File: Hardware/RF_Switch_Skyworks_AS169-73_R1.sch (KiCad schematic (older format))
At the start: 5 parts, among them U7 AS169-73

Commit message: Added discrete Chebyshev input filter to schematic based on Qucs simulationd. Artwork not done. It has occurred to me that I need to do some major cleanup of the test points on this PCBA.
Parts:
- renumbered C42 to C41, C43 to C42, C44 to C43
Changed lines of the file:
@@
 $Descr A4 11693 8268
 encoding utf-8
-Sheet 12 12
+Sheet 12 16
 Title ""
 Date ""
@@
 AR Path="/5F20D989/5F02EBC3" Ref="#PWR?"  Part="1"
 AR Path="/5F20DB0B/5F02EBC3" Ref="#PWR?"  Part="1"
-AR Path="/5F2751D2/5F02EBC3" Ref="#PWR051"  Part="1"
-F 0 "#PWR051" H 5600 3850 50  0001 C CNN
+AR Path="/5F2751D2/5F02EBC3" Ref="#PWR048"  Part="1"
+F 0 "#PWR048" H 5600 3850 50  0001 C CNN
 F 1 "GNDA" H 5605 3927 50  0000 C CNN
 F 2 "" H 5600 4100 50  0001 C CNN
@@
 AR Path="/5F20D989/5F11A2FE" Ref="C?"  Part="1"
 AR Path="/5F20DB0B/5F11A2FE" Ref="C?"  Part="1"
-AR Path="/5F2751D2/5F11A2FE" Ref="C42"  Part="1"
-F 0 "C42" V 4498 3400 50  0000 C CNN
+AR Path="/5F2751D2/5F11A2FE" Ref="C41"  Part="1"
+F 0 "C41" V 4498 3400 50  0000 C CNN
 F 1 "600S101" V 4589 3400 50  0000 C CNN
 F 2 "Capacitor_SMD:C_0603_1608Metric" H 4800 3500 50  0001 C CNN
@@
 AR Path="/5F20D989/5F30C645" Ref="#PWR?"  Part="1"
 AR Path="/5F20DB0B/5F30C645" Ref="#PWR?"  Part="1"
-AR Path="/5F2751D2/5F30C645" Ref="#PWR052"  Part="1"
-F 0 "#PWR052" H 6900 2550 50  0001 C CNN
+AR Path="/5F2751D2/5F30C645" Ref="#PWR049"  Part="1"
+F 0 "#PWR049" H 6900 2550 50  0001 C CNN
 F 1 "GNDA" H 6905 2627 50  0000 C CNN
 F 2 "" H 6900 2800 50  0001 C CNN
@@
 AR Path="/5F20D989/5F30E7E0" Ref="C?"  Part="1"
 AR Path="/5F20DB0B/5F30E7E0" Ref="C?"  Part="1"
-AR Path="/5F2751D2/5F30E7E0" Ref="C43"  Part="1"
-F 0 "C43" V 6400 3700 50  0000 C CNN
+AR Path="/5F2751D2/5F30E7E0" Ref="C42"  Part="1"
+F 0 "C42" V 6400 3700 50  0000 C CNN
 F 1 "600S101" V 6500 3700 50  0000 C CNN
 F 2 "Capacitor_SMD:C_0603_1608Metric" H 6300 3800 50  0001 C CNN
@@
 J2
 $Comp
-L ATC:600S101_3-pad-R C44
+L ATC:600S101_3-pad-R C43
 U 1 1 5F334699
 P 6500 3300
-F 0 "C44" H 6150 3450 50  0000 L CNN
+F 0 "C43" H 6150 3450 50  0000 L CNN
 F 1 "600S101_3-pad-R" H 6150 3550 50  0000 L CNN
 F 2 "Capacitor_SMD:C_0603_1608Metric_3-pad-R" H 7400 2550 50  0001 C CNN

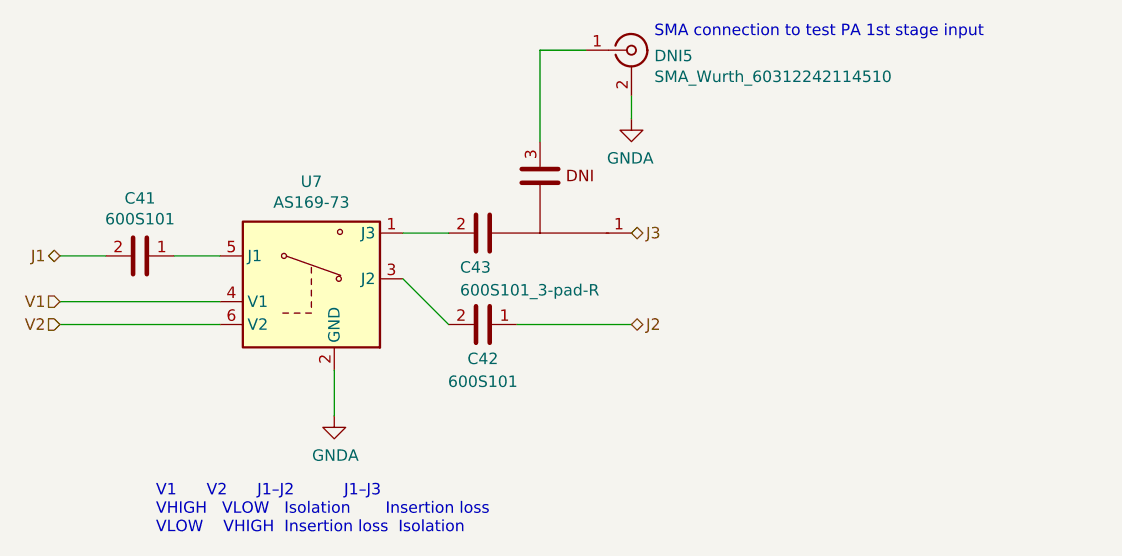
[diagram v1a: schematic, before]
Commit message: Major cleanup to both the schematic and directory structure. Stackup has changed accomodate to 0.65mm trace width. Chebyshev filter lived through the experience in the Qucs simulation; others not checked yet. I do want to re-visit the matching networks of all of the amplifiers as I have developed some good strategies to implement them.
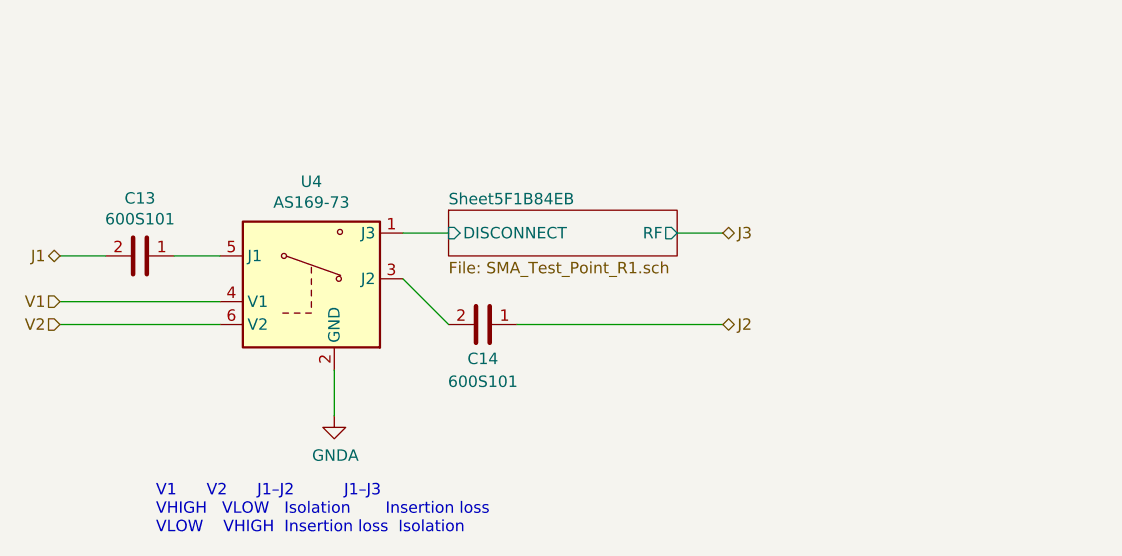
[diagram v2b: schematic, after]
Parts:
- removed C43: 600S101_3-pad-R, Capacitor_SMD:C_0603_1608Metric_3-pad-R, symbol ATC:600S101_3-pad-R
- removed DNI5: SMA_Wurth_60312242114510, RF:SMA_Wurth_60312242114510, symbol RF:SMA_Wurth_60312242114510
- renumbered C41 to C13, C42 to C14, U7 to U4
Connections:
- net Sheet5F1B84EB/DISCONNECT: now reaches U4.1 (J3)
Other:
- note removed: "SMA connection to test PA 1st stage input"
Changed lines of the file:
@@
 $Descr A4 11693 8268
 encoding utf-8
-Sheet 12 16
+Sheet 15 24
 Title ""
 Date ""
@@
 AR Path="/5F20D989/5F02EBC3" Ref="#PWR?"  Part="1"
 AR Path="/5F20DB0B/5F02EBC3" Ref="#PWR?"  Part="1"
-AR Path="/5F2751D2/5F02EBC3" Ref="#PWR048"  Part="1"
-F 0 "#PWR048" H 5600 3850 50  0001 C CNN
+AR Path="/5F2751D2/5F02EBC3" Ref="#PWR017"  Part="1"
+F 0 "#PWR017" H 5600 3850 50  0001 C CNN
 F 1 "GNDA" H 5605 3927 50  0000 C CNN
 F 2 "" H 5600 4100 50  0001 C CNN
@@
 AR Path="/5F20D989/5F064460" Ref="U?"  Part="1"
 AR Path="/5F20DB0B/5F064460" Ref="U?"  Part="1"
-AR Path="/5F2751D2/5F064460" Ref="U7"  Part="1"
-F 0 "U7" H 5500 3925 50  0000 C CNN
+AR Path="/5F2751D2/5F064460" Ref="U4"  Part="1"
+F 0 "U4" H 5500 3925 50  0000 C CNN
 F 1 "AS169-73" H 5500 3834 50  0000 C CNN
 F 2 "Package_TO_SOT_SMD:SOT-23-6" H 5600 3500 50  0001 C CNN
@@
 AR Path="/5F20D989/5F11A2FE" Ref="C?"  Part="1"
 AR Path="/5F20DB0B/5F11A2FE" Ref="C?"  Part="1"
-AR Path="/5F2751D2/5F11A2FE" Ref="C41"  Part="1"
-F 0 "C41" V 4498 3400 50  0000 C CNN
+AR Path="/5F2751D2/5F11A2FE" Ref="C13"  Part="1"
+F 0 "C13" V 4498 3400 50  0000 C CNN
 F 1 "600S101" V 4589 3400 50  0000 C CNN
 F 2 "Capacitor_SMD:C_0603_1608Metric" H 4800 3500 50  0001 C CNN
@@
 $EndComp
 Wire Wire Line
-	6700 2500 6500 2500
-Text Notes 7000 2450 0    50   ~ 0
-SMA connection to test PA 1st stage input
-$Comp
-L RF:SMA_Wurth_60312242114510 DNI?
-U 1 1 5F30C63E
-P 6900 2500
-AR Path="/5F20DB0B/5F30C63E" Ref="DNI?"  Part="1"
-AR Path="/5F20A94F/5F30C63E" Ref="DNI?"  Part="1"
-AR Path="/5F2751D2/5F30C63E" Ref="DNI5"  Part="1"
-F 0 "DNI5" H 7000 2475 50  0000 L CNN
-F 1 "SMA_Wurth_60312242114510" H 7000 2384 50  0000 L CNN
-F 2 "RF:SMA_Wurth_60312242114510" H 6900 2500 50  0001 C CNN
-F 3 "https://www.we-online.de/katalog/datasheet/60312242114510.pdf" H 6900 2500 50  0001 C CNN
-	1    6900 2500
-	1    0    0    -1
-$EndComp
-$Comp
-L power:GNDA #PWR?
-U 1 1 5F30C645
-P 6900 2800
-AR Path="/5F1FE880/5F30C645" Ref="#PWR?"  Part="1"
-AR Path="/5F19C733/5F30C645" Ref="#PWR?"  Part="1"
-AR Path="/5F19DDB3/5F30C645" Ref="#PWR?"  Part="1"
-AR Path="/5F11BFA6/5F30C645" Ref="#PWR?"  Part="1"
-AR Path="/5F11C68E/5F30C645" Ref="#PWR?"  Part="1"
-AR Path="/5F20A94F/5F30C645" Ref="#PWR?"  Part="1"
-AR Path="/5F20D989/5F30C645" Ref="#PWR?"  Part="1"
-AR Path="/5F20DB0B/5F30C645" Ref="#PWR?"  Part="1"
-AR Path="/5F2751D2/5F30C645" Ref="#PWR049"  Part="1"
-F 0 "#PWR049" H 6900 2550 50  0001 C CNN
-F 1 "GNDA" H 6905 2627 50  0000 C CNN
-F 2 "" H 6900 2800 50  0001 C CNN
-F 3 "" H 6900 2800 50  0001 C CNN
-	1    6900 2800
-	-1   0    0    -1
-$EndComp
-Wire Wire Line
-	6900 2700 6900 2800
-Wire Wire Line
-	6500 2500 6500 2900
-Wire Wire Line
 	5900 3500 6100 3700
-Text HLabel 6900 3300 2    50   BiDi ~ 0
+Text HLabel 7300 3300 2    50   BiDi ~ 0
 J3
-Wire Wire Line
-	6400 3700 6900 3700
 $Comp
 L ATC:600S101 C?
@@
 AR Path="/5F20D989/5F30E7E0" Ref="C?"  Part="1"
 AR Path="/5F20DB0B/5F30E7E0" Ref="C?"  Part="1"
-AR Path="/5F2751D2/5F30E7E0" Ref="C42"  Part="1"
-F 0 "C42" V 6400 3700 50  0000 C CNN
+AR Path="/5F2751D2/5F30E7E0" Ref="C14"  Part="1"
+F 0 "C14" V 6400 3700 50  0000 C CNN
 F 1 "600S101" V 6500 3700 50  0000 C CNN
 F 2 "Capacitor_SMD:C_0603_1608Metric" H 6300 3800 50  0001 C CNN
@@
 	0    1    1    0
 $EndComp
-Text HLabel 6900 3700 2    50   BiDi ~ 0
+Text HLabel 7300 3700 2    50   BiDi ~ 0
 J2
-$Comp
-L ATC:600S101_3-pad-R C43
-U 1 1 5F334699
-P 6500 3300
-F 0 "C43" H 6150 3450 50  0000 L CNN
-F 1 "600S101_3-pad-R" H 6150 3550 50  0000 L CNN
-F 2 "Capacitor_SMD:C_0603_1608Metric_3-pad-R" H 7400 2550 50  0001 C CNN
-F 3 "" V 6500 3250 50  0001 C CNN
-	1    6500 3300
-	1    0    0    1
-$EndComp
+Wire Wire Line
+	6400 3700 7300 3700
+Wire Wire Line
+	7100 3300 7300 3300
+$Sheet
+S 6100 3200 1000 200
+U 5F1B84EC
+F0 "Sheet5F1B84EB" 50
+F1 "SMA_Test_Point_R1.sch" 50
+F2 "DISCONNECT" I L 6100 3300 50
+F3 "RF" O R 7100 3300 50
+$EndSheet
 $EndSCHEMATC

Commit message: Improving LNA simulations and Documentation package. More to come on this one.
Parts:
- renumbered C13 to C16, C14 to C17
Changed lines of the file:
@@
 $Descr A4 11693 8268
 encoding utf-8
-Sheet 15 24
+Sheet 8 23
 Title ""
 Date ""
@@
 AR Path="/5F20D989/5F02EBC3" Ref="#PWR?"  Part="1"
 AR Path="/5F20DB0B/5F02EBC3" Ref="#PWR?"  Part="1"
-AR Path="/5F2751D2/5F02EBC3" Ref="#PWR017"  Part="1"
-F 0 "#PWR017" H 5600 3850 50  0001 C CNN
+AR Path="/5F2751D2/5F02EBC3" Ref="#PWR019"  Part="1"
+F 0 "#PWR019" H 5600 3850 50  0001 C CNN
 F 1 "GNDA" H 5605 3927 50  0000 C CNN
 F 2 "" H 5600 4100 50  0001 C CNN
@@
 AR Path="/5F20D989/5F11A2FE" Ref="C?"  Part="1"
 AR Path="/5F20DB0B/5F11A2FE" Ref="C?"  Part="1"
-AR Path="/5F2751D2/5F11A2FE" Ref="C13"  Part="1"
-F 0 "C13" V 4498 3400 50  0000 C CNN
+AR Path="/5F2751D2/5F11A2FE" Ref="C16"  Part="1"
+F 0 "C16" V 4498 3400 50  0000 C CNN
 F 1 "600S101" V 4589 3400 50  0000 C CNN
 F 2 "Capacitor_SMD:C_0603_1608Metric" H 4800 3500 50  0001 C CNN
@@
 AR Path="/5F20D989/5F30E7E0" Ref="C?"  Part="1"
 AR Path="/5F20DB0B/5F30E7E0" Ref="C?"  Part="1"
-AR Path="/5F2751D2/5F30E7E0" Ref="C14"  Part="1"
-F 0 "C14" V 6400 3700 50  0000 C CNN
+AR Path="/5F2751D2/5F30E7E0" Ref="C17"  Part="1"
+F 0 "C17" V 6400 3700 50  0000 C CNN
 F 1 "600S101" V 6500 3700 50  0000 C CNN
 F 2 "Capacitor_SMD:C_0603_1608Metric" H 6300 3800 50  0001 C CNN
